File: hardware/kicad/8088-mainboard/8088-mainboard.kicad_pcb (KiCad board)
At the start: 2 copper layers, 149 x 90 mm, 62 parts, among them J1 Exp0, J2 POWER 5v, J3 Exp1, J4 Exp2, SW1 Reset, U1 8088, U10 74LS273, U11 74LS00, U12 74LS138, U13 HM62256BLP, U2 8284, U3 74LS373, U4 74LS373, U5 74LS245, U6 8288, U7 74LS138, U8 28C256, U9 HM62256BLP, Y1 14.31818 MHz

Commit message: Add PSB board design
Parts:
- removed J4: Exp2, Connector_IDC:IDC-Header_2x20_P2.54mm_Vertical
- removed R5, R6, R7, R8: 10k, Resistor_THT:R_Axial_DIN0207_L6.3mm_D2.5mm_P7.62mm_Horizontal
- added J_DEBUG1: DEBUG, Connector_PinHeader_2.54mm:PinHeader_1x10_P2.54mm_Vertical, F.Cu at (113.2, 25.6)
- moved SW1 143.0 mm to (165.1, 30.1), turned to 180 degrees
- moved C4 127.8 mm to (151.7, 28.8), turned to 90 degrees
- moved R1 106.2 mm to (144.8, 25.1), turned to -90 degrees
- moved U12 68.0 mm to (139.4, 136.6)
- moved C16 67.6 mm to (133.7, 129.0)
- moved U7 66.1 mm to (139.4, 121.6)
- moved C10 65.7 mm to (133.7, 113.9)
- moved C17 44.6 mm to (133.7, 88.8), turned to -90 degrees
- moved U3 44.2 mm to (102.7, 75.8)
- moved U13 43.1 mm to (139.4, 104.1), turned to 90 degrees
- moved R9 40.1 mm to (51.2, 68.2), turned to -90 degrees
- moved C6 39.7 mm to (102.2, 63.0), turned to 0 degrees
- moved R10 39.4 mm to (48.2, 68.2), turned to -90 degrees
- moved R11 38.7 mm to (45.1, 68.2), turned to -90 degrees
- moved R12 38.0 mm to (42.1, 68.2), turned to -90 degrees
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- renumbered J2 to J1, J1 to J2
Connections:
- J2 pad 1: VCC -> GND
- J2 pad 10: /A7 -> /D0
- J2 pad 11: /A8 -> /A1
- J2 pad 12: /A9 -> /A0
- J2 pad 13: /A10 -> /A3
- J2 pad 14: /A11 -> /A2
- J2 pad 15: /A12 -> /A5
- J2 pad 16: /A13 -> /A4
- J2 pad 17: /A14 -> /A7
- J2 pad 18: /A15 -> /A6
- J2 pad 19: /A16 -> /A9
- J2 pad 2: GND -> VCC
- J2 pad 20: /A17 -> /A8
- J2 pad 21: /A18 -> /A11
- J2 pad 22: /A19 -> /A10
- J2 pad 23: /D0 -> /A13
- J2 pad 24: /D1 -> /A12
- J2 pad 25: /D2 -> /A15
- J2 pad 26: /D3 -> /A14
- J2 pad 27: /D4 -> /A17
- J2 pad 28: /D5 -> /A16
- J2 pad 29: /D6 -> /A19
- J2 pad 3: /A0 -> /D7
- J2 pad 30: /D7 -> /A18
- J2 pad 31: /MRDC -> /IORC
- J2 pad 32: /MWTC -> /IOWC
- J2 pad 33: /IORC -> /MRDC
- J2 pad 34: /IOWC -> /MWTC
- J2 pad 35: /MEM_DECODER/MEM_80000_9FFFF -> /RESET
- J2 pad 36: /IO_DECODER/IO_A0_BF -> /ALE
- J2 pad 37: /CLK -> GND
- J2 pad 38: /ALE -> /CLK
- J2 pad 39: /RESET -> /IO_DECODER/IO_A0_BF
- J2 pad 4: /A1 -> /D6
- J2 pad 40: GND -> /MEM_DECODER/MEM_80000_9FFFF
- J2 pad 5: /A2 -> /D5
- J2 pad 6: /A3 -> /D4
- J2 pad 7: /A4 -> /D3
- J2 pad 8: /A5 -> /D2
- J2 pad 9: /A6 -> /D1
- J3 pad 1: VCC -> GND
- J3 pad 10: /A7 -> /D0
- J3 pad 11: /A8 -> /A1
- J3 pad 12: /A9 -> /A0
- J3 pad 13: /A10 -> /A3
- J3 pad 14: /A11 -> /A2
- J3 pad 15: /A12 -> /A5
- J3 pad 16: /A13 -> /A4
- J3 pad 17: /A14 -> /A7
- J3 pad 18: /A15 -> /A6
- J3 pad 19: /A16 -> /A9
- J3 pad 2: GND -> VCC
- J3 pad 20: /A17 -> /A8
- J3 pad 21: /A18 -> /A11
- J3 pad 22: /A19 -> /A10
- J3 pad 23: /D0 -> /A13
- J3 pad 24: /D1 -> /A12
- J3 pad 25: /D2 -> /A15
- J3 pad 26: /D3 -> /A14
- J3 pad 27: /D4 -> /A17
- J3 pad 28: /D5 -> /A16
- J3 pad 29: /D6 -> /A19
- J3 pad 3: /A0 -> /D7
- J3 pad 30: /D7 -> /A18
- J3 pad 31: /MRDC -> /IORC
- J3 pad 32: /MWTC -> /IOWC
- J3 pad 33: /IORC -> /MRDC
- J3 pad 34: /IOWC -> /MWTC
- J3 pad 35: /MEM_DECODER/MEM_A0000_BFFFF -> /RESET
- J3 pad 36: /IO_DECODER/IO_C0_DF -> /ALE
- J3 pad 37: /CLK -> GND
- J3 pad 38: /ALE -> /CLK
- J3 pad 39: /RESET -> /IO_DECODER/IO_C0_DF
- J3 pad 4: /A1 -> /D6
- J3 pad 40: GND -> /MEM_DECODER/MEM_A0000_BFFFF
- J3 pad 5: /A2 -> /D5
- J3 pad 6: /A3 -> /D4
- J3 pad 7: /A4 -> /D3
- J3 pad 8: /A5 -> /D2
- J3 pad 9: /A6 -> /D1
- U1 pad 17: Net-(U1-NMI) -> GND
- U1 pad 18: Net-(U1-INTR) -> GND
- U1 pad 23: Net-(U1-~{TEST}) -> GND
- U1 pad 31: Net-(U1-HOLD) -> GND
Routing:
- net VCC: track 0.00 -> 651.2 mm, vias 0 -> 17
- net /A7: track 0.00 -> 303.5 mm, vias 0 -> 3
- net /D1: track 0.00 -> 302.2 mm, vias 0 -> 3
- net /D5: track 0.00 -> 299.6 mm, vias 0 -> 1
- net /D4: track 0.00 -> 292.5 mm, vias 0 -> 3
- net /D0: track 0.00 -> 286.5 mm, vias 0 -> 3
- net /D3: track 0.00 -> 277.1 mm, vias 0 -> 3
- net /D7: track 0.00 -> 274.6 mm, vias 0 -> 1
- net /D6: track 0.00 -> 266.9 mm, vias 0 -> 1
- net /A10: track 0.00 -> 262.5 mm, vias 0 -> 3
- net /A6: track 0.00 -> 257.2 mm, vias 0 -> 2
- net /A11: track 0.00 -> 254.8 mm, vias 0 -> 4
- net /D2: track 0.00 -> 253.1 mm, vias 0 -> 3
- net /A0: track 0.00 -> 251.7 mm, vias 0 -> 4
- net /A9: track 0.00 -> 247.0 mm, vias 0 -> 2
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- added copper zone on B.Cu, net GND
- added copper zone on F.Cu, net GND
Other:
- board size 149 x 90 mm -> 160 x 126 mm
- board text added: "+5v"
- board text added: "8088 CPU"
- board text added: "8088 Mainboard"
- board text added: "ALE"
- board text added: "BIOS ROM"
- board text added: "CLK"
- board text added: "DEBUG LEDs"
- board text added: "DEN"
- board text added: "EXT0"
- board text added: "EXT1"
- board text added: "GND"
- board text added: "I/O DECODER"
- board text added: "IORC"
- board text added: "IOWC"
- board text added: "MEM DECODER"
- board text added: "MRDC"
- board text added: "MWTC"
- board text added: "PWD"
- board text added: "Project: github.com/i-melnichenko/8088-homebrew-computer"
- board text added: "RAM BANK0"
- board text added: "RAM BANK1"
- board text added: "READY"
- board text added: "RES"
- board text added: "RESET"
- board text added: "RST"
- board text added: "Rev. 1.0"

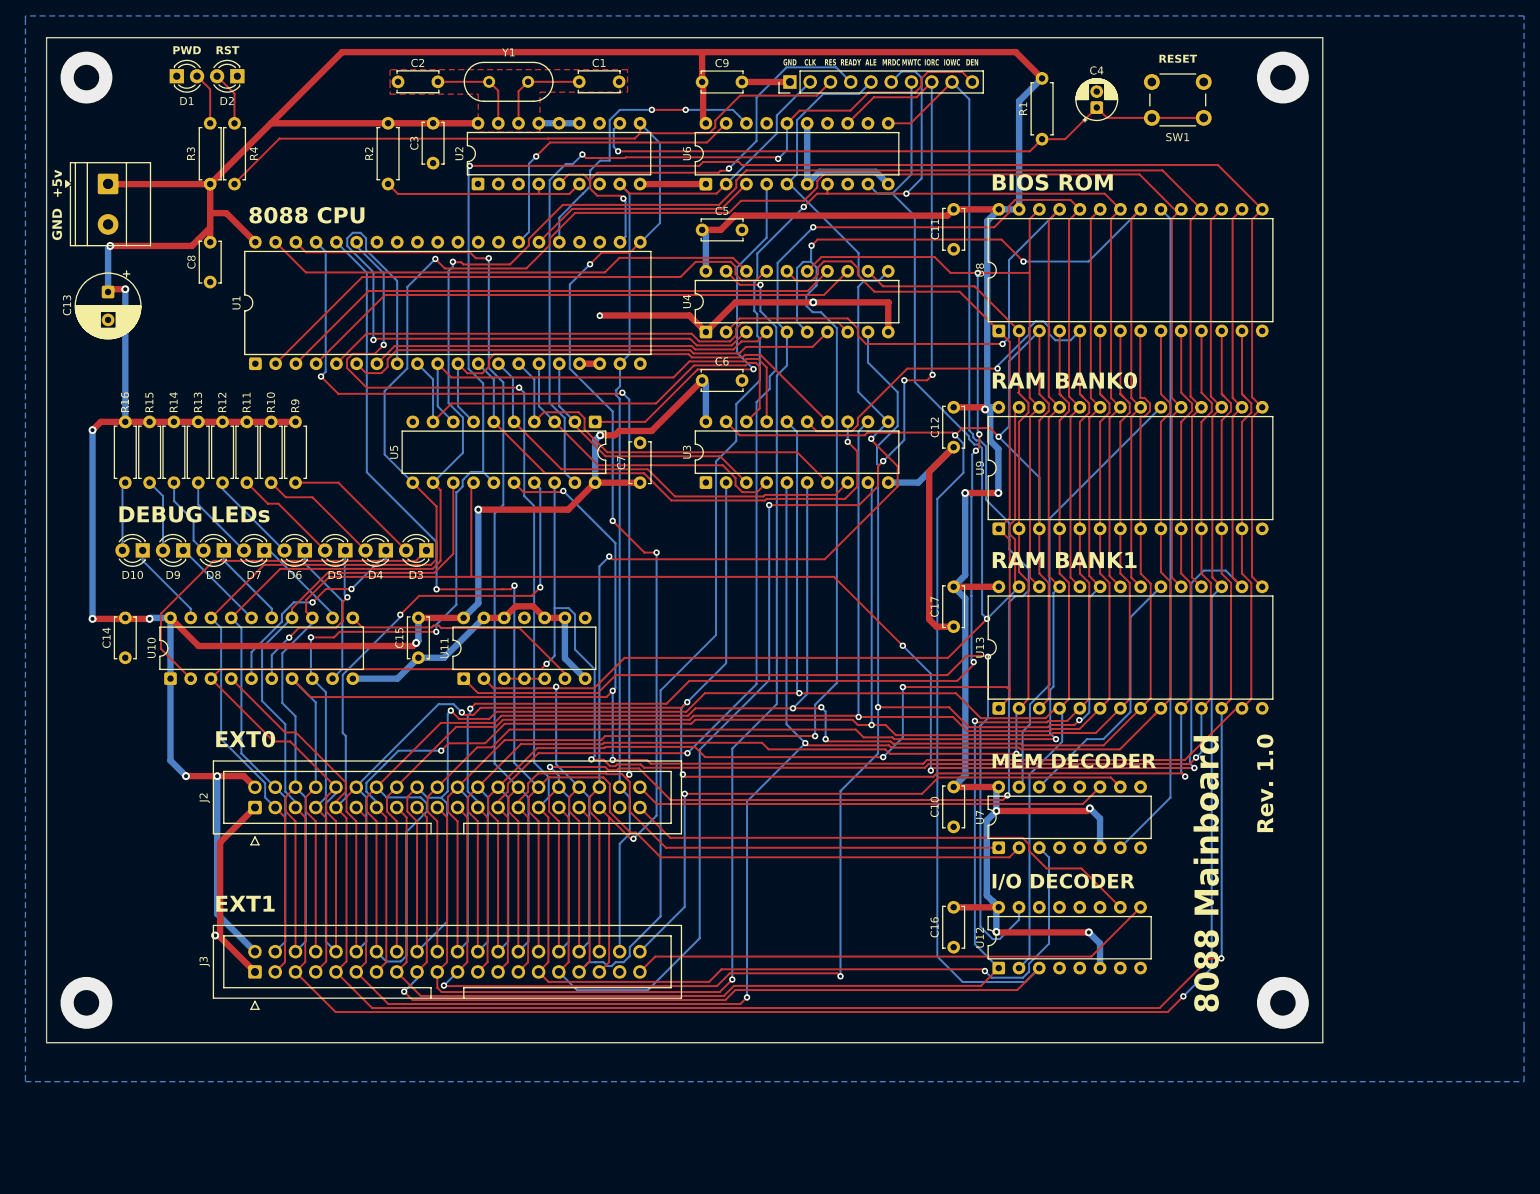
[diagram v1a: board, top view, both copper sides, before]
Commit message: Update 8088-mainboard schematics for refined connections and label adjustments
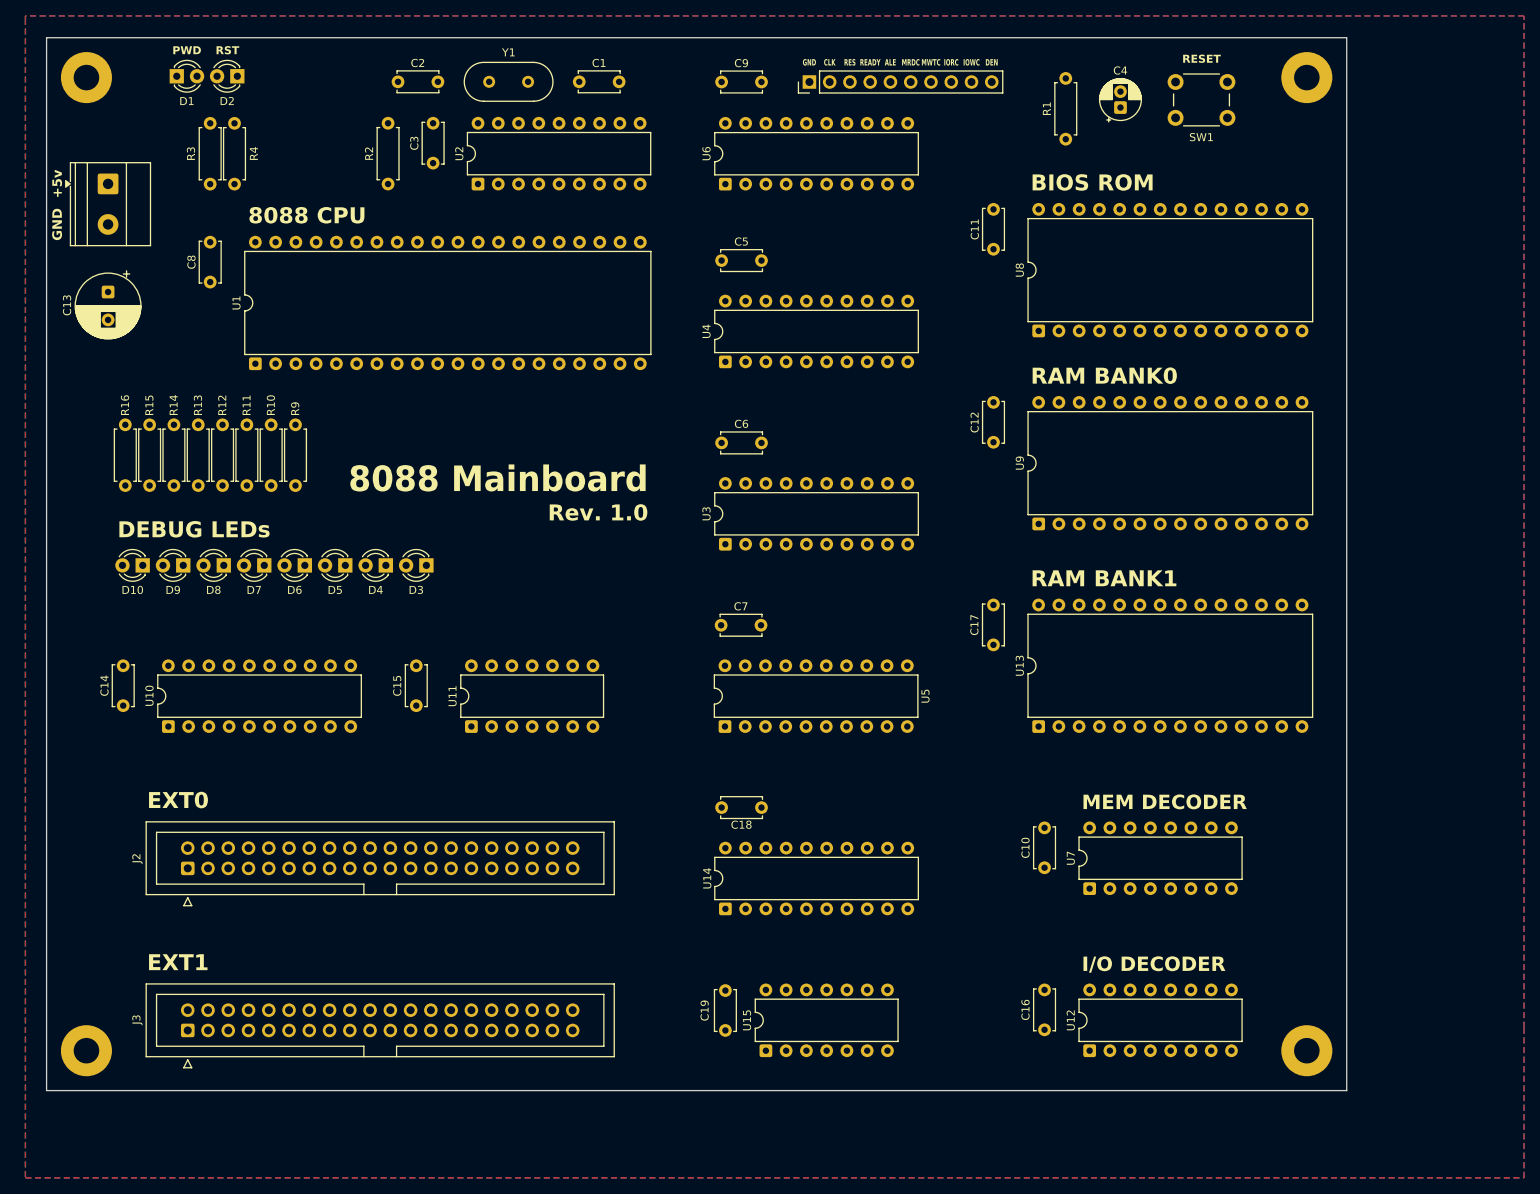
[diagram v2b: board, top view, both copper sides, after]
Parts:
- added C18: 100nF, Capacitor_THT:C_Disc_D5.0mm_W2.5mm_P5.00mm, F.Cu at (104.6, 116.5)
- added C19: 100nF, Capacitor_THT:C_Disc_D5.0mm_W2.5mm_P5.00mm, F.Cu at (105.1, 144.5)
- added H1: MountingHole_Pad, MountingHole:MountingHole_3.2mm_M3_Pad, F.Cu at (25.0, 25.0)
- added H2: MountingHole_Pad, MountingHole:MountingHole_3.2mm_M3_Pad, F.Cu at (178.0, 25.0)
- added H3: MountingHole_Pad, MountingHole:MountingHole_3.2mm_M3_Pad, F.Cu at (25.0, 147.0)
- added H4: MountingHole_Pad, MountingHole:MountingHole_3.2mm_M3_Pad, F.Cu at (178.0, 147.0)
- added U14: 74LS373, Package_DIP:DIP-20_W7.62mm, F.Cu at (105.1, 129.2)
- added U15: 74LS00, Package_DIP:DIP-14_W7.62mm, F.Cu at (110.2, 147.0)
- moved U5 41.5 mm to (105.1, 106.4), turned to 90 degrees
- moved C7 20.6 mm to (104.6, 93.7), turned to 0 degrees
- moved C16 15.4 mm to (145.1, 139.4)
- moved U12 15.4 mm to (150.8, 147.0)
- moved C10 12.5 mm to (145.1, 119.1)
- moved U7 12.5 mm to (150.8, 126.7)
- moved J2 11.4 mm to (37.7, 124.1)
- moved J3 11.2 mm to (37.7, 144.5)
- moved C6 8.20 mm to (104.6, 70.8)
- moved U3 8.10 mm to (105.1, 83.5)
- moved U11 6.08 mm to (73.3, 106.4)
- moved C14 6.01 mm to (29.6, 98.7)
- moved C15 6.01 mm to (66.4, 98.7)
- moved U10 6.01 mm to (35.3, 106.4)
- moved C17 5.49 mm to (138.7, 91.1)
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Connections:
- net /IO_DECODER/IO_A0_BF renamed /EXPANSION_CONNECTOR/IO_EXP0_CS
- net /IO_DECODER/IO_C0_DF renamed /EXPANSION_CONNECTOR/IO_EXP1_CS
- net /MEM_DECODER/MEM_00000_1FFFF renamed /MEM_DECODER/RAM_BANK0_CS
- net /MEM_DECODER/MEM_20000_3FFFF renamed /MEM_DECODER/RAM_BANK1_CS
- net /MEM_DECODER/MEM_80000_9FFFF renamed /EXPANSION_CONNECTOR/MEM_EXP0_CS
- net /MEM_DECODER/MEM_A0000_BFFFF renamed /EXPANSION_CONNECTOR/MEM_EXP1_CS
- net /MEM_DECODER/MEM_E0000_FFFFF renamed /MEM_DECODER/ROM_CS
- U1 pad 25: /CPU/S2 -> unconnected-(U1-ALE-Pad25)
- U1 pad 26: /CPU/S1 -> /CPU/S0
- U1 pad 27: /CPU/S0 -> /CPU/S1
- U1 pad 28: /CPU/IOM -> /CPU/S2
- U1 pad 29: /CPU/WR -> unconnected-(U1-~{WR}-Pad29)
- U1 pad 31: GND -> unconnected-(U1-HOLD-Pad31)
- U1 pad 32: /CPU/RD -> unconnected-(U1-~{RD}-Pad32)
- U1 pad 35: /A19 -> /CPU/AD19
- U1 pad 36: /A18 -> /CPU/AD18
- U1 pad 37: /A17 -> /CPU/AD17
- U1 pad 38: /A16 -> /CPU/AD16
- U11 pad 1: /IO_DECODER/IO_00_1F -> /IO_DECODER/LED_PANEL_CS
- U11 pad 10: GND -> /IOWC
- U11 pad 2: /MWTC -> /IO_DECODER/LED_PANEL_CS
- U11 pad 5: Net-(U11-Pad3) -> Net-(U11-Pad5)
- U11 pad 8: unconnected-(U11-Pad8) -> Net-(U11-Pad5)
- U11 pad 9: GND -> /IOWC
- U12 pad 11: /IO_DECODER/IO_80_9F -> unconnected-(U12-O4-Pad11)
- U12 pad 12: /IO_DECODER/IO_60_7F -> unconnected-(U12-O3-Pad12)
- U12 pad 13: /IO_DECODER/IO_40_5F -> unconnected-(U12-O2-Pad13)
- U12 pad 14: /IO_DECODER/IO_20_3F -> unconnected-(U12-O1-Pad14)
- U12 pad 15: /IO_DECODER/IO_00_1F -> /IO_DECODER/LED_PANEL_CS
- U12 pad 6: VCC -> /IO_DEC_EN
- U12 pad 7: /IO_DECODER/IO_E0_FF -> unconnected-(U12-O7-Pad7)
- U2 pad 12: /CLOCK/OSC -> unconnected-(U2-OSC-Pad12)
- U2 pad 2: /CLOCK/PCLK -> unconnected-(U2-PCLK-Pad2)
- U6 pad 12: /CPU/AIOWC -> unconnected-(U6-~{AIOWC}-Pad12)
- U6 pad 14: /CPU/INTA -> unconnected-(U6-~{INTA}-Pad14)
- U6 pad 15: GND -> VCC
- U6 pad 16: /CPU/DEN -> Net-(U6-DEN)
- U6 pad 8: /CPU/AMWC -> unconnected-(U6-~{AMWC}-Pad8)
- U7 pad 12: /MEM_DECODER/MEM_60000_7FFFF -> unconnected-(U7-O3-Pad12)
- U7 pad 13: /MEM_DECODER/MEM_40000_5FFFF -> unconnected-(U7-O2-Pad13)
- U7 pad 6: VCC -> /MEM_DEC_EN
- U7 pad 9: /MEM_DECODER/MEM_C0000_DFFFF -> unconnected-(U7-O6-Pad9)
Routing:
- net VCC: track 651.2 -> 0.00 mm, vias 17 -> 0
- net /A7: track 303.5 -> 0.00 mm, vias 3 -> 0
- net /D1: track 302.2 -> 0.00 mm, vias 3 -> 0
- net /D5: track 299.6 -> 0.00 mm, vias 1 -> 0
- net /D4: track 292.5 -> 0.00 mm, vias 3 -> 0
- net /D0: track 286.5 -> 0.00 mm, vias 3 -> 0
- net /D3: track 277.1 -> 0.00 mm, vias 3 -> 0
- net /D7: track 274.6 -> 0.00 mm, vias 1 -> 0
- net /D6: track 266.9 -> 0.00 mm, vias 1 -> 0
- net /A10: track 262.5 -> 0.00 mm, vias 3 -> 0
- net /A6: track 257.2 -> 0.00 mm, vias 2 -> 0
- net /A11: track 254.8 -> 0.00 mm, vias 4 -> 0
- net /D2: track 253.1 -> 0.00 mm, vias 3 -> 0
- net /A0: track 251.7 -> 0.00 mm, vias 4 -> 0
- net /A9: track 247.0 -> 0.00 mm, vias 2 -> 0
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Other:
- board size 160 x 126 mm -> 163 x 132 mm

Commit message: Update 8088-mainboard PCB
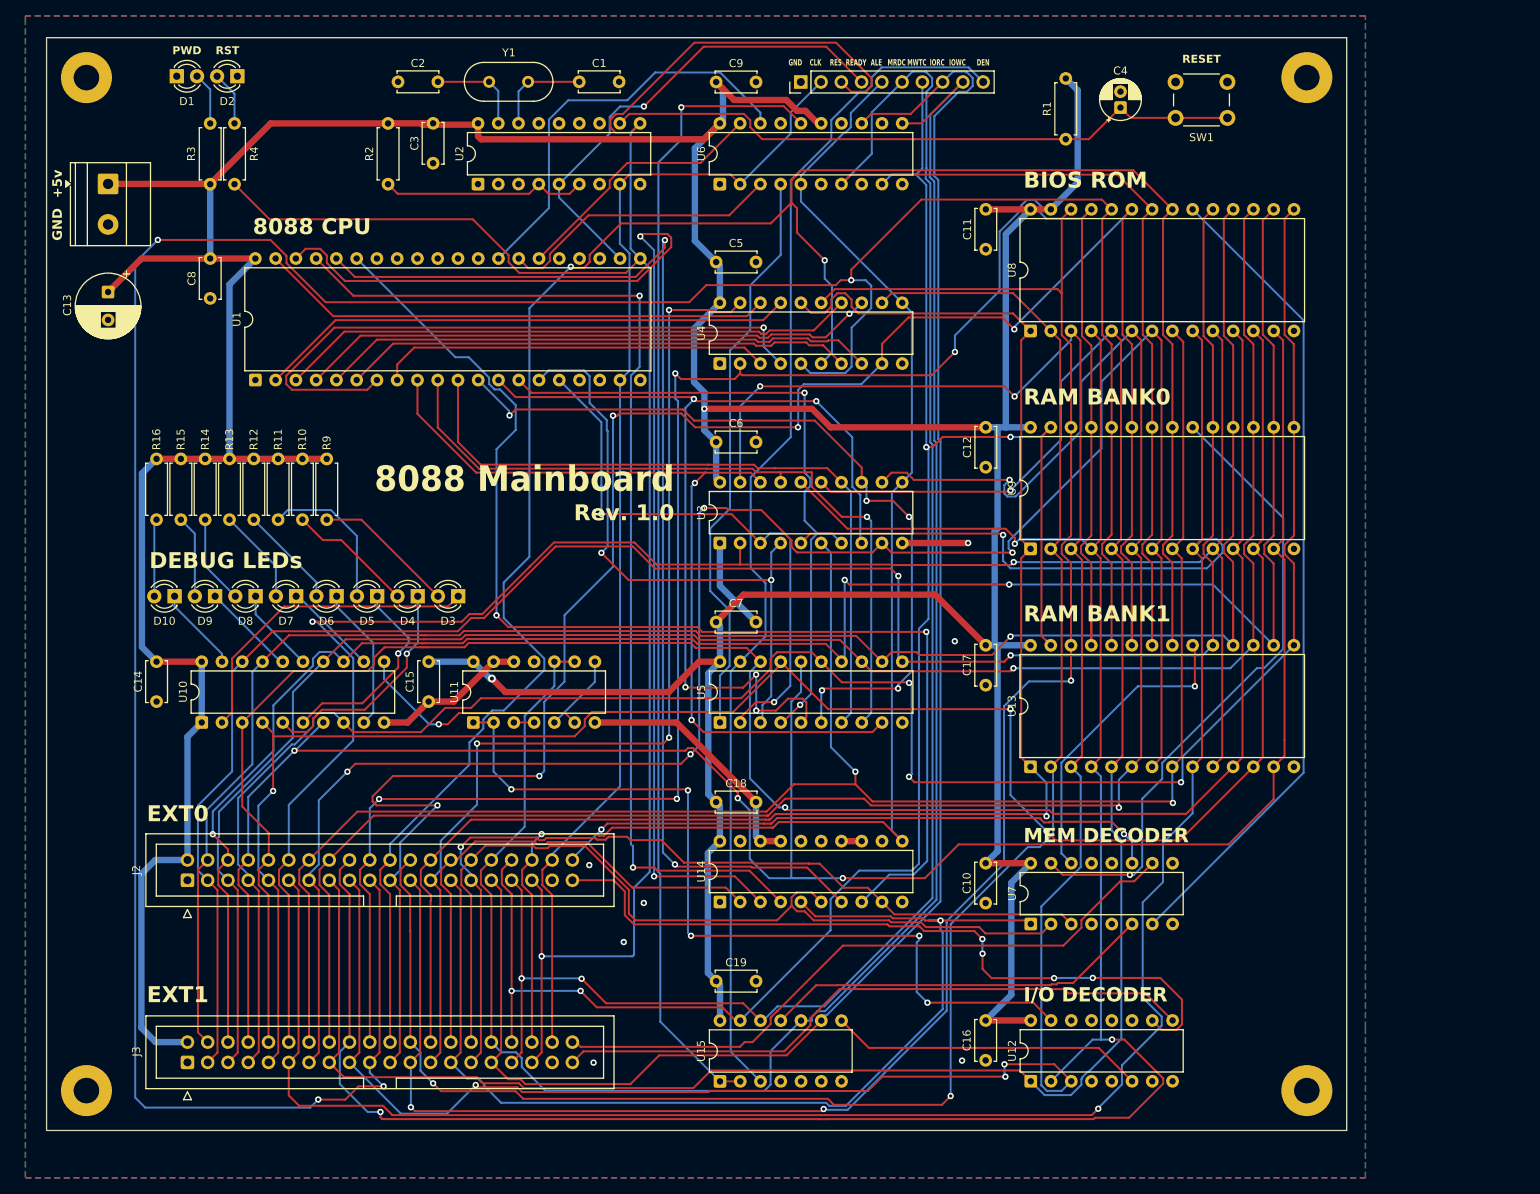
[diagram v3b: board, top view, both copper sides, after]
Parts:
- moved C10 8.61 mm to (137.7, 123.5)
- moved U7 8.61 mm to (143.4, 131.1)
- moved C16 8.32 mm to (137.7, 143.2)
- moved U12 8.32 mm to (143.4, 150.8)
- moved U15 6.92 mm to (104.4, 150.8)
- moved C19 6.29 mm to (103.9, 138.3), turned to 0 degrees
- moved R11 5.80 mm to (49.0, 72.8)
- moved R12 5.80 mm to (46.0, 72.8)
- moved R15 5.80 mm to (36.8, 72.8)
- moved R16 5.80 mm to (33.8, 72.8)
- moved R10 5.80 mm to (52.1, 72.8)
- moved R13 5.80 mm to (42.9, 72.8)
- moved R14 5.80 mm to (39.9, 72.8)
- moved R9 5.80 mm to (55.1, 72.8)
- moved D10 5.56 mm to (36.0, 90.0)
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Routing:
- net VCC: track 0.00 -> 644.8 mm, vias 0 -> 2
- net /A9: track 0.00 -> 377.5 mm, vias 0 -> 4
- net /MRDC: track 0.00 -> 311.2 mm, vias 0 -> 2
- net /A1: track 0.00 -> 301.3 mm, vias 0 -> 2
- net /A6: track 0.00 -> 287.9 mm, vias 0 -> 3
- net /A7: track 0.00 -> 283.6 mm, vias 0 -> 5
- net /A10: track 0.00 -> 277.8 mm, vias 0 -> 2
- net /D2: track 0.00 -> 275.0 mm, vias 0 -> 3
- net /A5: track 0.00 -> 272.7 mm, vias 0 -> 1
- net /A11: track 0.00 -> 260.3 mm, vias 0 -> 5
- net /D3: track 0.00 -> 258.9 mm, vias 0 -> 3
- net /A8: track 0.00 -> 255.7 mm, vias 0 -> 4
- net /D7: track 0.00 -> 252.7 mm, vias 0 -> 2
- net /A3: track 0.00 -> 251.0 mm, vias 0 -> 4
- net /D1: track 0.00 -> 250.5 mm, vias 0 -> 3
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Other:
- board size 163 x 132 mm -> 163 x 137 mm
